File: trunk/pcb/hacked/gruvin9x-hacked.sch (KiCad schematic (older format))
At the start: 148 parts, among them P1 CONN_5X2, P2 CONN_5, P3 CONN_6, P4 CONN_9, P5 CONN_9, P6 CONN_6, P7 CONN_12, P8 CONN_30, Q1 2SC9014, SW1 SW_PUSH, SW2 SW_PUSH, SW3 SW_PUSH, SW4 SW_PUSH, SW5 SW_PUSH, SW6 SW_PUSH, U1 78L05, U2 4066, U3 LN-6206-30, X1 16MHz

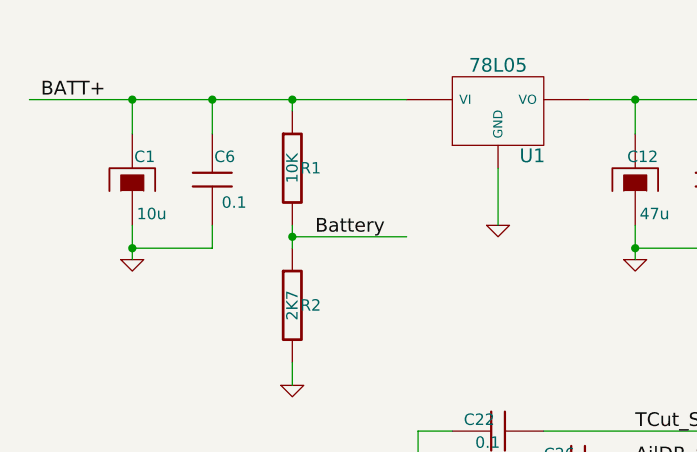
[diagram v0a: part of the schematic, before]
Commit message: Added Turnigy 9X V2 backup firmware to allow restoring of original V2 factory firmware. (This firmware as supplied by http://HobbyKing.com)
Corrected error in all circuit schematic versiosn -- R1 is a 5K1, not a 10K.
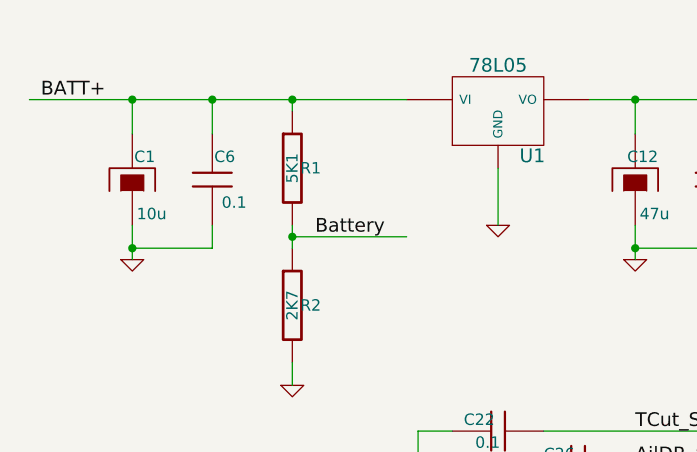
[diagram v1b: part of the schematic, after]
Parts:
- R1: value 10K -> 5K1
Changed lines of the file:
@@
-EESchema Schematic File Version 2  date 26/11/2010 9:52:37 a.m.
+EESchema Schematic File Version 2  date 14/12/2010 1:53:56 p.m.
 LIBS:power
 LIBS:device
@@
 LIBS:contrib
 LIBS:valves
+LIBS:gruvin9x-hacked-cache
 EELAYER 24  0
 EELAYER END
@@
 Sheet 1 1
 Title "Main Controller PCB (Stock)"
-Date "25 nov 2010"
+Date "14 dec 2010"
 Rev "1.1"
 Comp "gruvin9x"
@@
 P 1750 1250
 F 0 "R1" H 1830 1250 50  0000 C CNN
-F 1 "10K" V 1750 1250 50  0000 C CNN
+F 1 "5K1" V 1750 1250 50  0000 C CNN
 	1    1750 1250
 	1    0    0    -1

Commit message: Gruvins hacked 9X radio circuitry as at 2010-12-26
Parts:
- removed D?: DIODE, symbol DIODE
- removed PX: CONN_3, symbol CONN_3
- removed Q?: NPN, symbol NPN
- removed R?: 33K, symbol R
- removed R? (x2): 10K, symbol R
- added HD1: DIODE, symbol DIODE
- added HR10: 330, symbol R
- added HR3, HR4, HR5, HR6, HR7: 10K, symbol R
- added HR8: 4K7, symbol R
- added HR9: 150K, symbol R
- added K1: CONN_3, symbol CONN_3
- added Q2: BC847C, SOT23-BCE, symbol BC847C
- added Q3: BC857C, SOT23-BCE, symbol BC857C
- added Q?: BC549, SOT23EBD, symbol NPN
- added R74: 1K, symbol R
- renumbered RH1 to HR1, RH1 to HR2
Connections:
- net labels added: TELEM_TX
- net labels removed: FrSky_RXD
- wire segments 468 -> 488
- no-connect marks 7 -> 6
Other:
- note added: "(0V/+5V TX)"
- note added: "(Pseudo)\nRS-232 TRX"
- note added: "(SIL3 hot-glued \nto main PCB)\n"
- note added: "PPM-in compatibility mod\nmake ... PPMIN=MOD1"
- note removed: "INPUT: Fr-Sky RXD converted to TTL\nSIL3 hot-glued to main PCB\n"
- note removed: "RS-232 +/12V"
- moved on the sheet: C10, C18, C19, C2, C22, C23, C24, C25, C26, C27, C28, C29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
